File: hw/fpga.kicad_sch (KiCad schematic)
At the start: 20 parts, among them U601 TPS7A2025PDQN, U602 ICE40UP5K-SG48ITR, X601 XC8102AA01NR-G, Y601 ECS-TXO-2016-33-400-TR

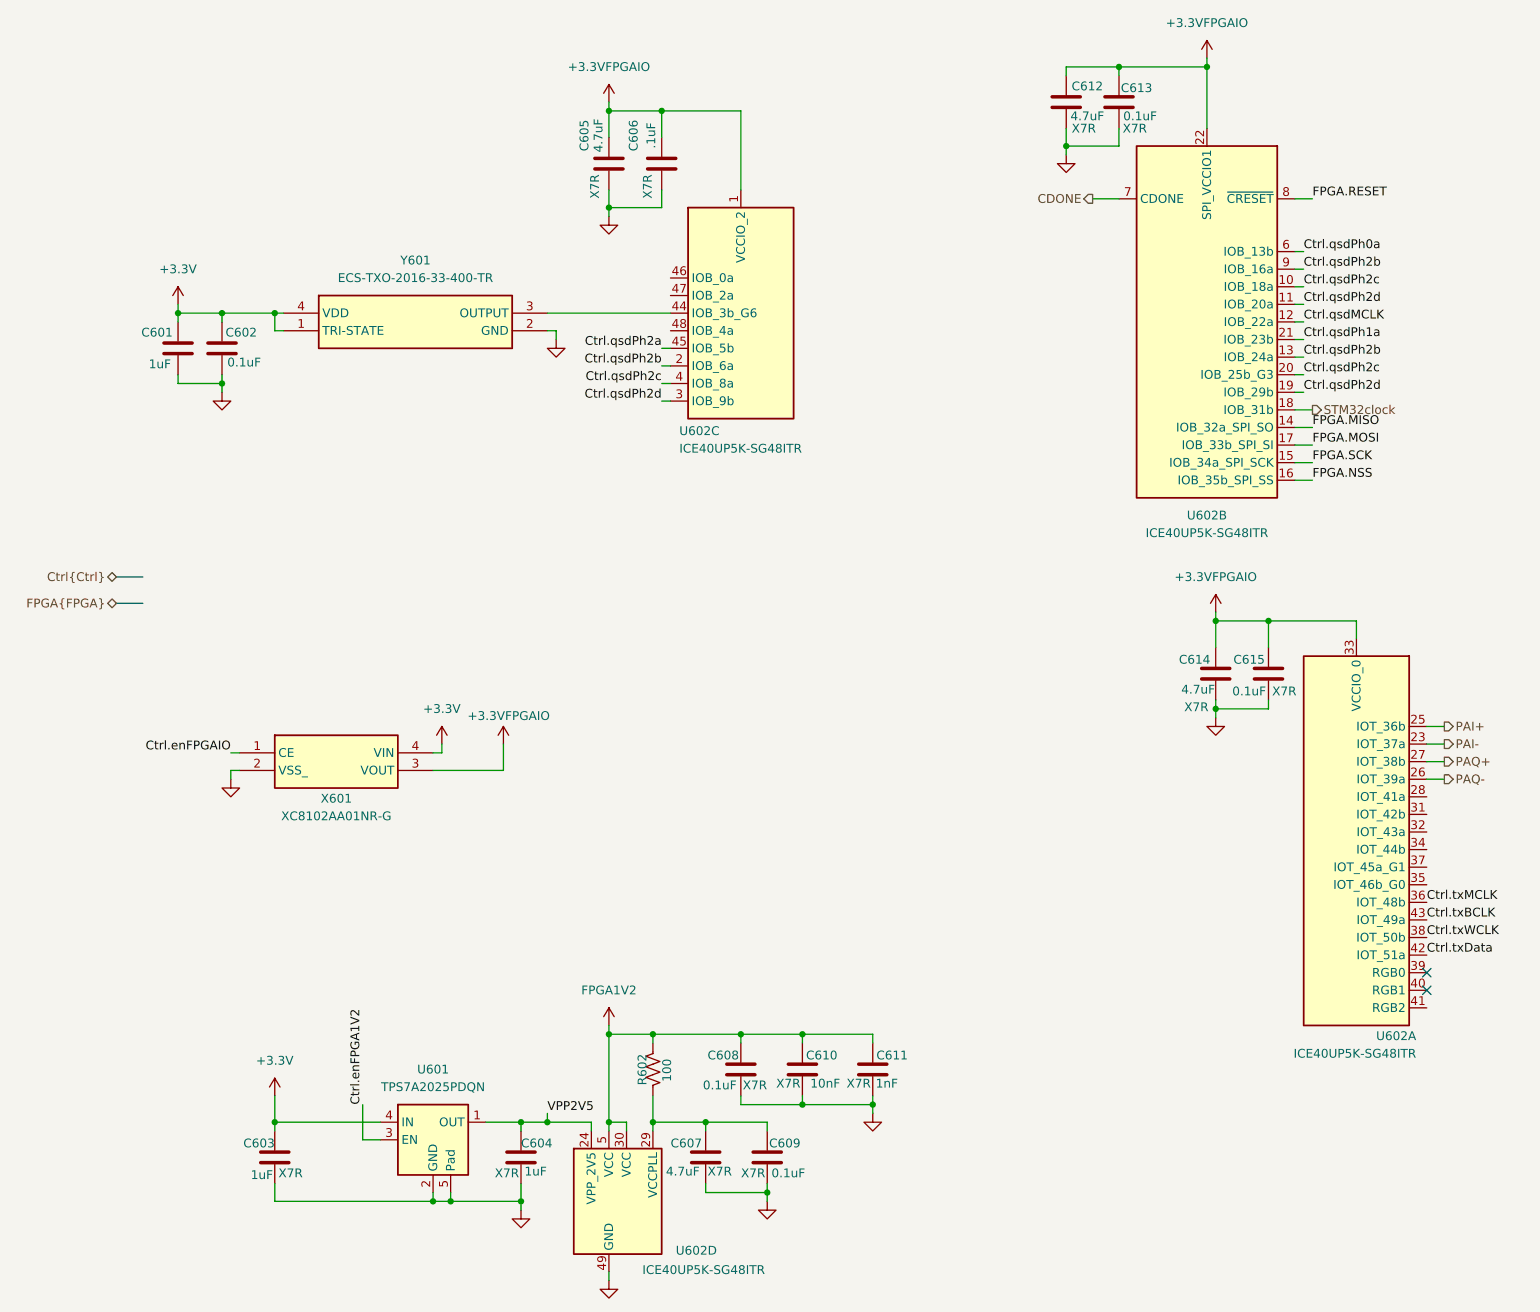
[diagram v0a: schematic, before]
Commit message: Schematic capture of the USBPD and +12V (+12V has priority) power scheme is "done". Have started working on RF deck mezzanine module but not yet divorced into another project
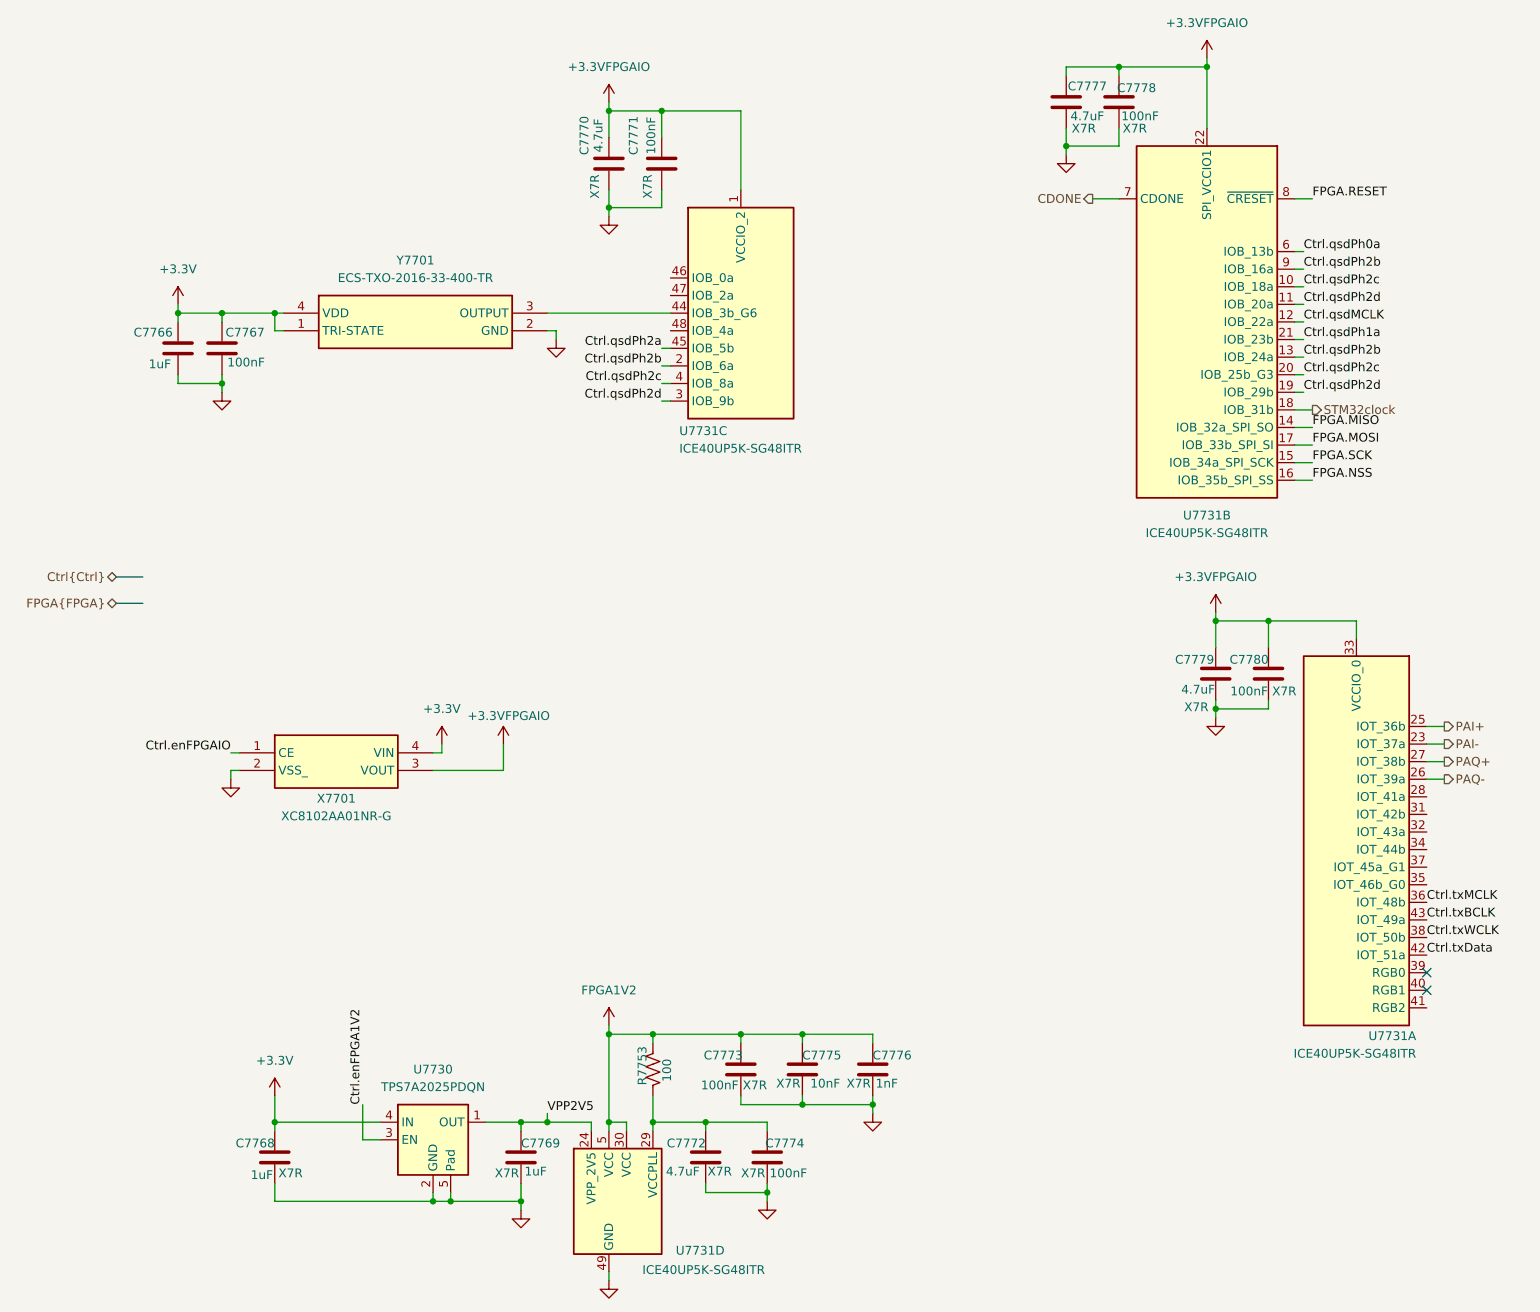
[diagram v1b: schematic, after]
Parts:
- C7767: renamed from C602; value 0.1uF -> 100nF
- C7771: renamed from C606; value .1uF -> 100nF
- C7773: renamed from C608; value 0.1uF -> 100nF
- C7774: renamed from C609; value 0.1uF -> 100nF
- C7778: renamed from C613; value 0.1uF -> 100nF
- C7780: renamed from C615; value 0.1uF -> 100nF
- renumbered C601 to C7766, C603 to C7768, C604 to C7769, C605 to C7770, C607 to C7772, C610 to C7775, C611 to C7776, C612 to C7777, C614 to C7779, R602 to R7753, U601 to U7730, U602 to U7731, X601 to X7701, Y601 to Y7701

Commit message: Last rites for 800 ohm rx preselector, and probably the RF deck which was stillborn
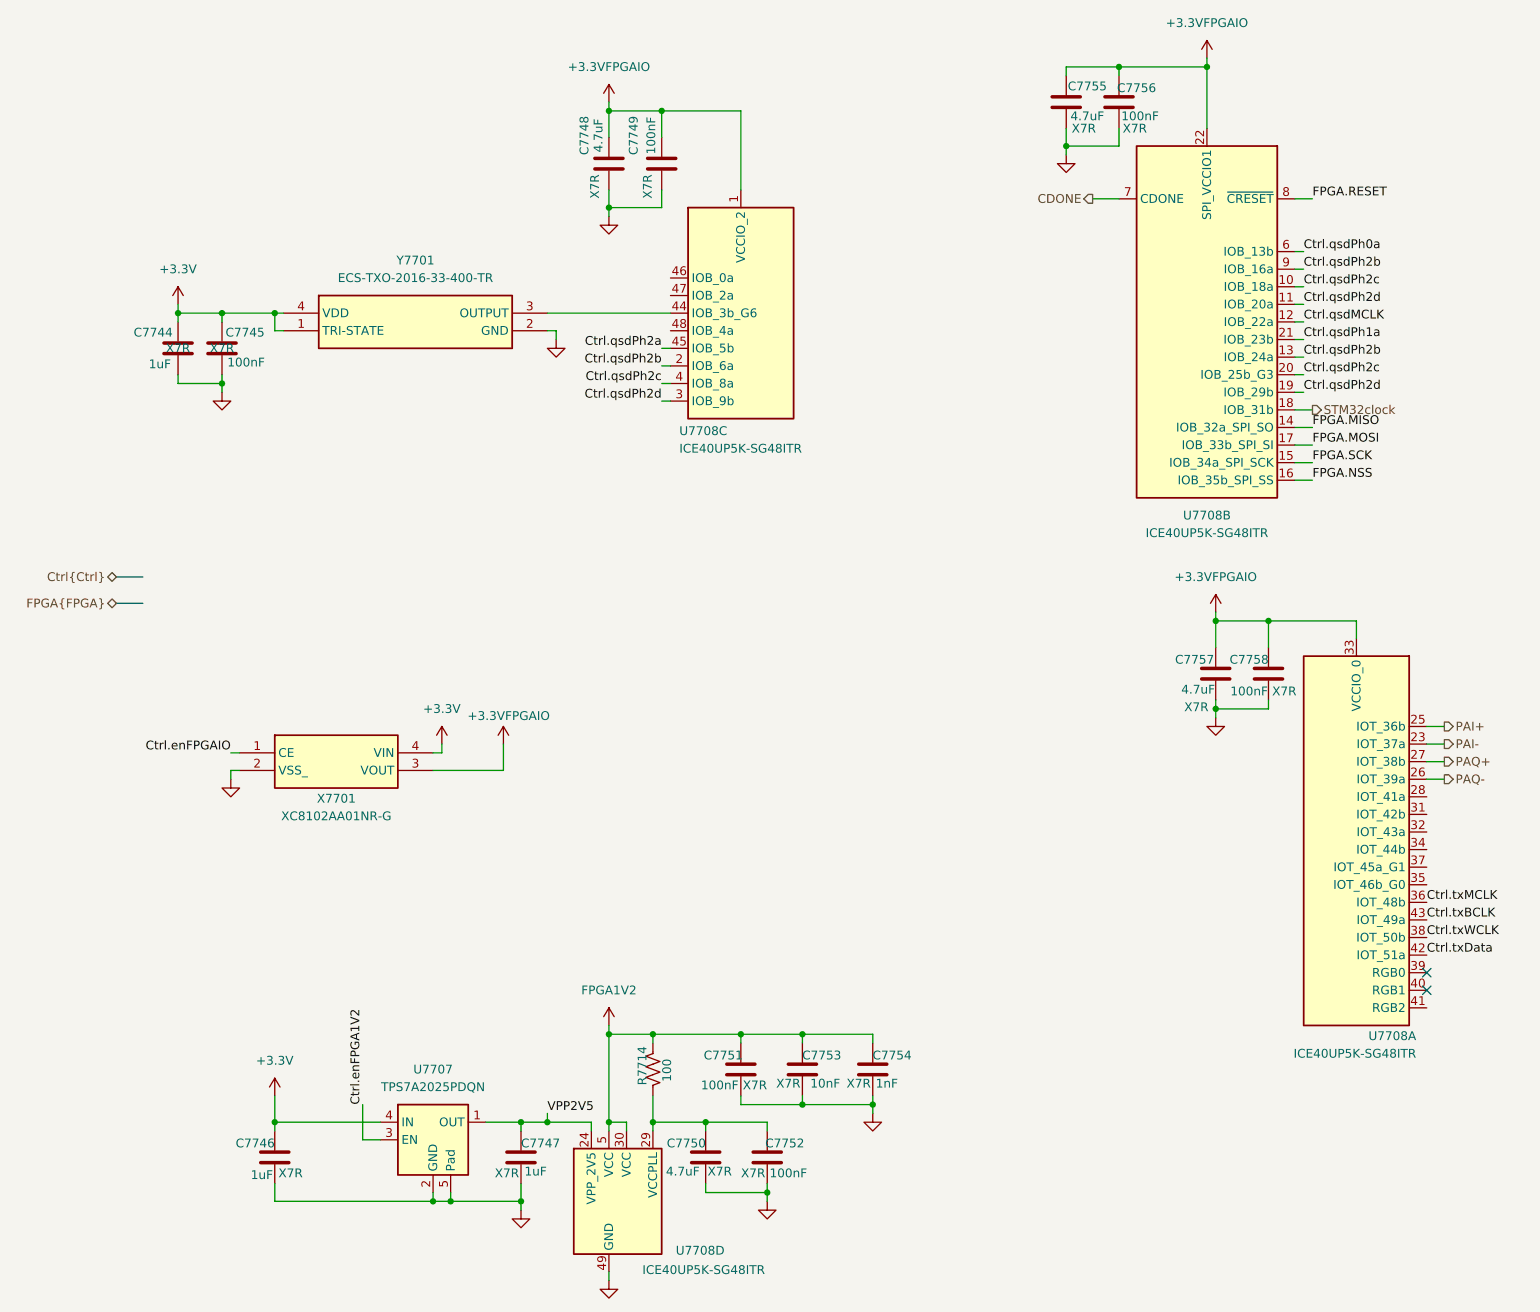
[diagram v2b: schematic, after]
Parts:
- C7744: renamed from C7766; cap-type (none) -> X7R
- C7745: renamed from C7767; cap-type (none) -> X7R
- C7754: renamed from C7776; footprint Capacitor_SMD:C_0805_2012Metric -> Capacitor_SMD:C_0201_0603Metric
- renumbered C7768 to C7746, C7769 to C7747, C7770 to C7748, C7771 to C7749, C7772 to C7750, C7773 to C7751, C7774 to C7752, C7775 to C7753, C7777 to C7755, C7778 to C7756, C7779 to C7757, C7780 to C7758, R7753 to R7714, U7730 to U7707, U7731 to U7708

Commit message: Fixed GPIO assignments. Fixed symbol for GRL2-2 relays.
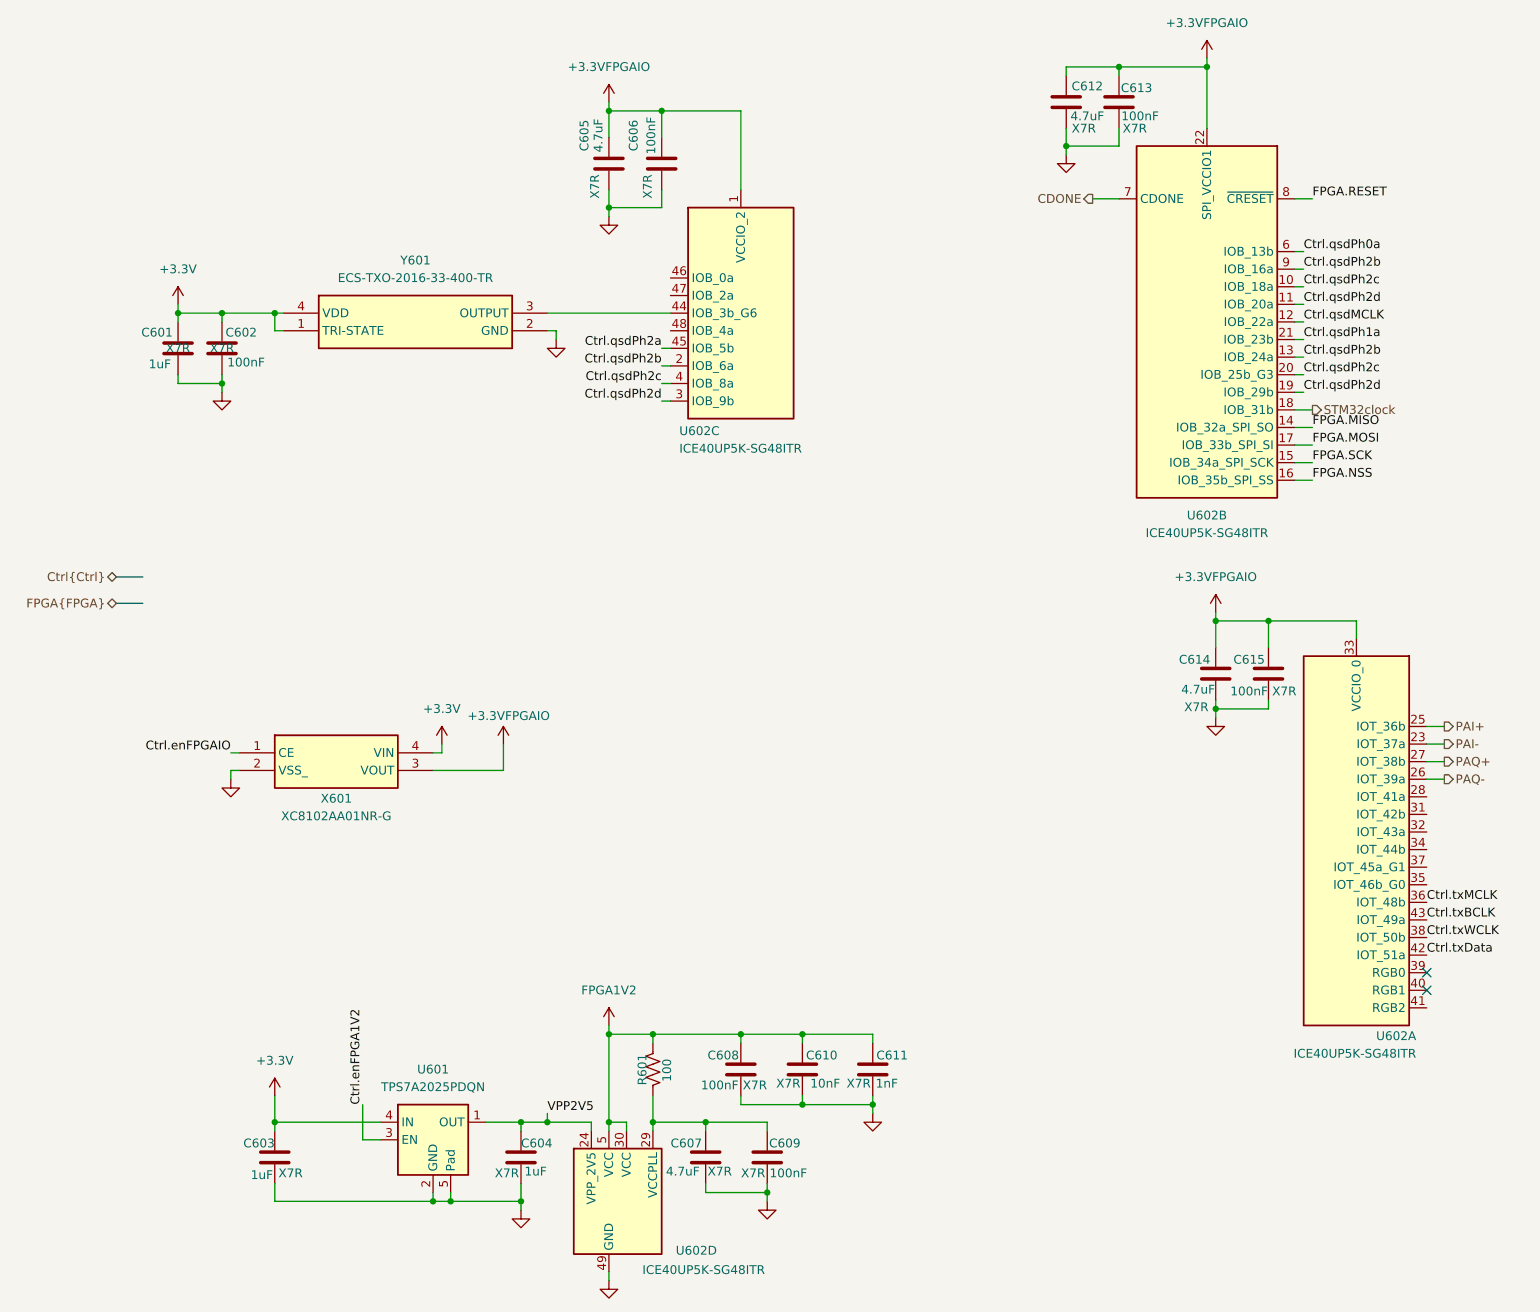
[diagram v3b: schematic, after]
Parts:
- C601: renamed from C7744; working-voltage (none) -> 50V
- C602: renamed from C7745; working-voltage (none) -> 50V
- C603: renamed from C7746; working-voltage (none) -> 50V
- C604: renamed from C7747; working-voltage (none) -> 50V
- C605: renamed from C7748; working-voltage (none) -> 10V
- C606: renamed from C7749; working-voltage (none) -> 50V
- C607: renamed from C7750; working-voltage (none) -> 10V
- C608: renamed from C7751; working-voltage (none) -> 50V
- C609: renamed from C7752; working-voltage (none) -> 50V
- C610: renamed from C7753; working-voltage (none) -> 25V
- C611: renamed from C7754; working-voltage (none) -> 25V
- C612: renamed from C7755; working-voltage (none) -> 10V
- C613: renamed from C7756; working-voltage (none) -> 50V
- C614: renamed from C7757; working-voltage (none) -> 10V
- C615: renamed from C7758; working-voltage (none) -> 50V
- renumbered R7714 to R601, U7707 to U601, U7708 to U602, X7701 to X601, Y7701 to Y601

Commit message: I think I have finished the relay conversion and 5V SPI I/O expander crap
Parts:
- renumbered C601 to C7759, C602 to C7760, C603 to C7761, C604 to C7762, C605 to C7763, C606 to C7764, C607 to C7765, C608 to C7766, C609 to C7767, C610 to C7768, C611 to C7769, C612 to C7770, C613 to C7771, C614 to C7772, C615 to C7773, R601 to R7723, U601 to U7709, U602 to U7710, X601 to X7701, Y601 to Y7701

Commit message: Starting to build guanella transformers. Mostly converted to 1-2-1 tx, but FPGA still to do.
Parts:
- removed unit 3 of U7710
- removed unit 2 of U7710
- removed unit 1 of U7710
- added C7780: 4.7uF, Capacitor_SMD:C_0805_2012Metric, symbol Device:C
- added C7781: 100nF, Capacitor_SMD:C_0805_2012Metric, symbol Device:C
- added U7713: ECP5-LFE5U-12, Package_QFP:TQFP-144_20x20mm_P0.5mm, symbol Library:LFE5U-12-TQFP144
- renumbered C7759 to C7765, C7760 to C7766, C7761 to C7767, C7762 to C7768, C7763 to C7769, C7764 to C7770, C7765 to C7771, C7766 to C7772, C7767 to C7773, C7768 to C7774, C7769 to C7775, C7770 to C7776, C7771 to C7777, C7772 to C7778, C7773 to C7779, U7709 to U7711, U7710 to U7712
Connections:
- net +3.3VFPGAIO: now also C7780.1, C7781.1, U7713.137 (VCCIO0)
- net GND: now also C7780.2, C7781.2, U7713.101 (GND), U7713.123 (GND), U7713.129 (GND), U7713.131 (GND), U7713.138 (GND), U7713.15 (GND), U7713.21 (GND), U7713.42 (GND), U7713.65 (GND), U7713.75 (GND), U7713.8 (GND), U7713.85 (GND), U7713.87 (GND)
- no-connect marks 2 -> 4
